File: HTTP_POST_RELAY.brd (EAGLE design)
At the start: 100 x 100 mm, 28 parts, among them IC1 ATMEGA328V-10P, IC2 7805T, IC3 ULN2003AN, Q1 16M

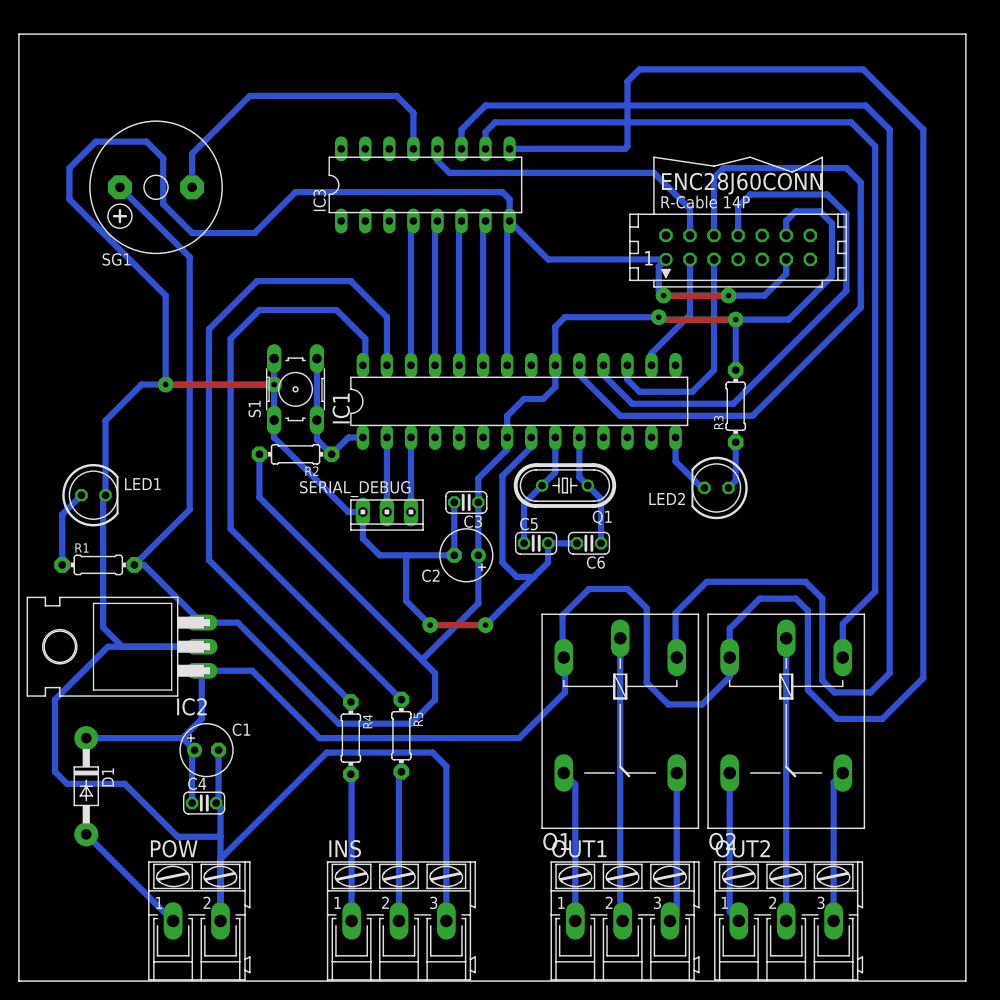
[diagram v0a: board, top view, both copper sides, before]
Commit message: add microcontroller firmware
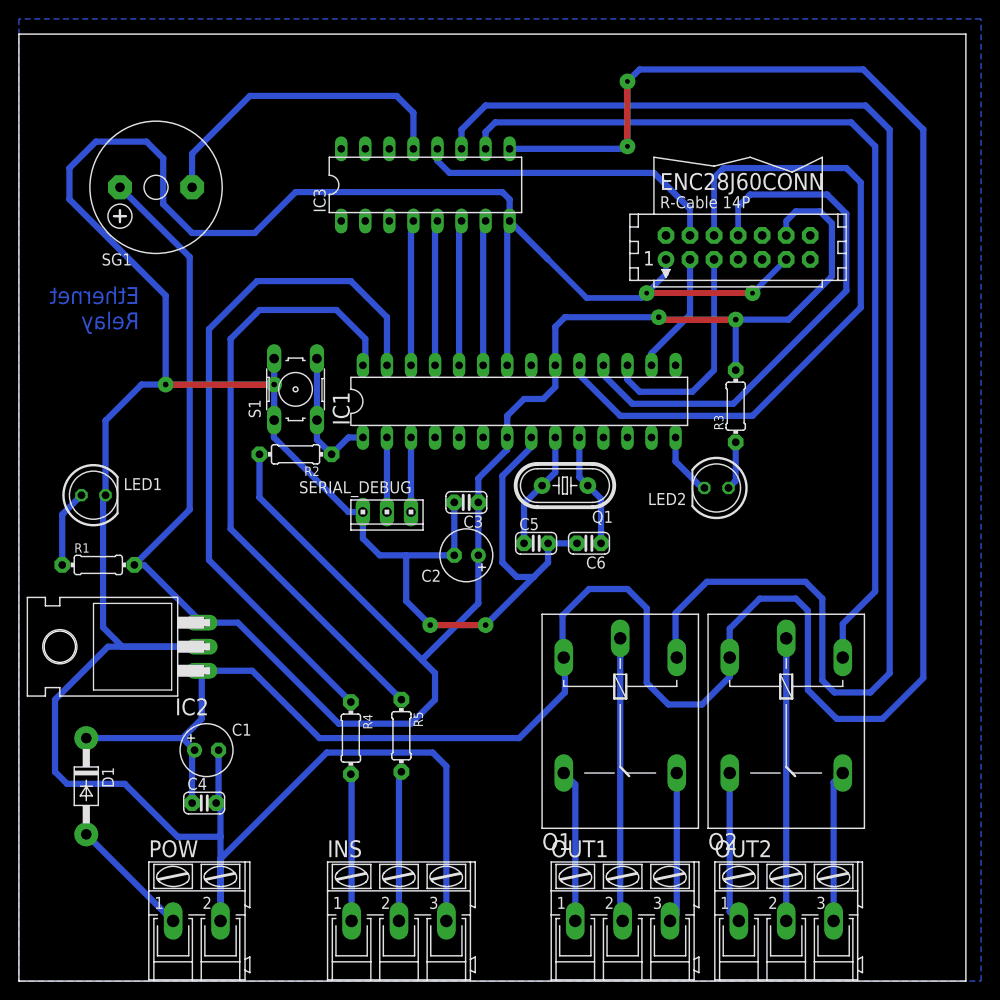
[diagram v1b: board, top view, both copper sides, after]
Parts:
- Q1: device crystal:HC49/S -> crystal:HC49U-V
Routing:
- net GND: track 394.7 -> 395.6 mm
- net +12V: vias 0 -> 2
- added copper zone on layer 16, net GND
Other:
- board text added: "Ethernet Relay"
